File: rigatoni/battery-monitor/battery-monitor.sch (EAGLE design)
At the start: 35 parts, among them J1 S2B-XH-A_(LF)(SN), J2 XF2C-2555-41A, J4 S4B-XH-A(LF)(SN), U1 LT1930ES5TRMPBF_BOOST_CONV, U2 ETH-POE, U3 STM32H743ZIT6

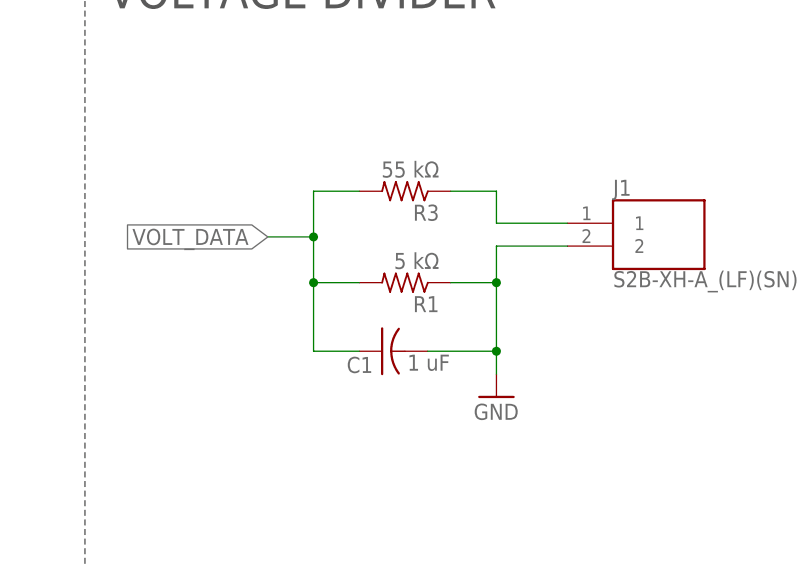
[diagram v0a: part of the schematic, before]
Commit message: Fix R1 value
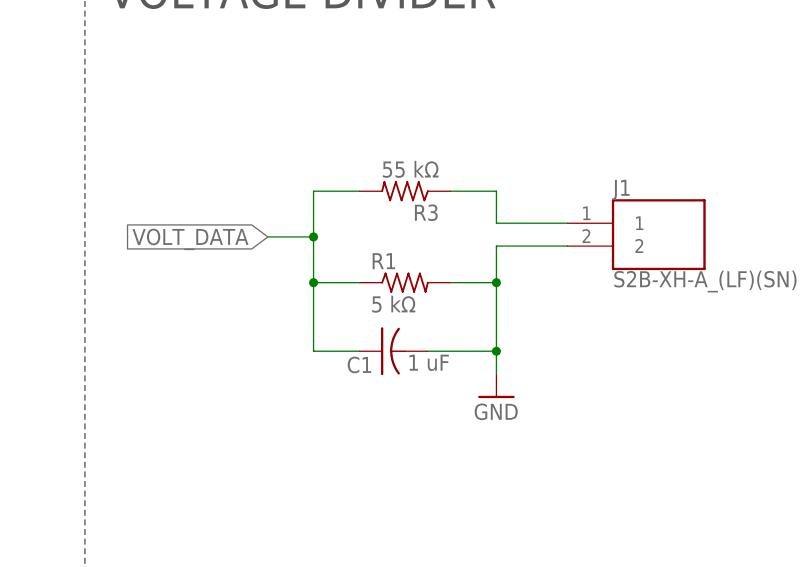
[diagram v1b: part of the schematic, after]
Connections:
- net GND: now also R1.2; no longer R1.1
- net VOLT_DATA: now also R1.1; no longer R1.2
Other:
- moved on the sheet: R1
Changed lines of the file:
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@@
 <setting verticaltext="up"/>
 </settings>
-<grid distance="0.1" unitdist="inch" unit="inch" style="lines" multiple="1" display="yes" altdistance="0.01" altunitdist="inch" altunit="inch"/>
+<grid distance="0.1" unitdist="inch" unit="inch" style="lines" multiple="1" display="no" altdistance="0.01" altunitdist="inch" altunit="inch"/>
 <layers>
 <layer number="1" name="Top" color="4" fill="1" visible="no" active="no"/>
@@
 </part>
 <part name="U3" library="RoboRacing_STM" deviceset="STM32H743ZIT6" device=""/>
-<part name="R1" library="rcl" library_urn="urn:adsk.eagle:library:334" deviceset="R-US_" device="R0603" package3d_urn="urn:adsk.eagle:package:23555/3" value="5 kΩ"/>
 <part name="R3" library="rcl" library_urn="urn:adsk.eagle:library:334" deviceset="R-US_" device="R0603" package3d_urn="urn:adsk.eagle:package:23555/3" value="55 kΩ"/>
 <part name="J1" library="drive_brake" deviceset="S2B-XH-A_(LF)(SN)" device=""/>
@@
 <part name="C1" library="rcl" library_urn="urn:adsk.eagle:library:334" deviceset="C-US" device="C0603" package3d_urn="urn:adsk.eagle:package:23616/2" value="1 uF"/>
 <part name="J2" library="con-omron" library_urn="urn:adsk.eagle:library:167" deviceset="XF2*-25?" device="55-41A" package3d_urn="urn:adsk.eagle:package:9078/1" technology="C"/>
+<part name="R1" library="rcl" library_urn="urn:adsk.eagle:library:334" deviceset="R-US_" device="R0603" package3d_urn="urn:adsk.eagle:package:23555/3" value="5 kΩ"/>
 </parts>
 <sheets>
@@
 <attribute name="VALUE" x="385.8006" y="113.2586" size="2.0828" layer="96" ratio="6" rot="SR0"/>
 </instance>
-<instance part="R1" gate="G$1" x="264.16" y="25.4" smashed="yes" rot="R180">
-<attribute name="NAME" x="267.97" y="23.9014" size="1.778" layer="95" rot="R180"/>
-<attribute name="VALUE" x="267.97" y="28.702" size="1.778" layer="96" rot="R180"/>
-</instance>
 <instance part="R3" gate="G$1" x="264.16" y="35.56" smashed="yes" rot="R180">
 <attribute name="NAME" x="267.97" y="34.0614" size="1.778" layer="95" rot="R180"/>
@@
 <instance part="J2" gate="-25" x="342.9" y="-2.54" smashed="yes">
 <attribute name="NAME" x="345.44" y="-3.302" size="1.524" layer="95"/>
+</instance>
+<instance part="R1" gate="G$1" x="264.16" y="25.4" smashed="yes">
+<attribute name="NAME" x="260.35" y="26.8986" size="1.778" layer="95"/>
+<attribute name="VALUE" x="260.35" y="22.098" size="1.778" layer="96"/>
 </instance>
 </instances>
@@
 </segment>
 <segment>
-<pinref part="R1" gate="G$1" pin="1"/>
 <wire x1="269.24" y1="25.4" x2="274.32" y2="25.4" width="0.1524" layer="91"/>
 <pinref part="J1" gate="G$1" pin="2"/>
@@
 <wire x1="266.7" y1="17.78" x2="274.32" y2="17.78" width="0.1524" layer="91"/>
 <junction x="274.32" y="17.78"/>
+<pinref part="R1" gate="G$1" pin="2"/>
 </segment>
 </net>
@@
 <pinref part="R3" gate="G$1" pin="2"/>
 <wire x1="259.08" y1="35.56" x2="254" y2="35.56" width="0.1524" layer="91"/>
-<pinref part="R1" gate="G$1" pin="2"/>
 <wire x1="254" y1="35.56" x2="254" y2="30.48" width="0.1524" layer="91"/>
 <wire x1="254" y1="30.48" x2="254" y2="25.4" width="0.1524" layer="91"/>
@@
 <wire x1="254" y1="17.78" x2="259.08" y2="17.78" width="0.1524" layer="91"/>
 <pinref part="C1" gate="G$1" pin="1"/>
-</segment>
-<segment>
+<pinref part="R1" gate="G$1" pin="1"/>
+</segment>
+<segment>

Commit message: Removed Ethernet Header and MCU from schematic
Also updated RoboRacing_STM library
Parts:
- removed C14: 1uF, rcl:C-USC0603
- removed C15: 0.1uF, rcl:C-USC0603
- removed D6: 5.1V, SparkFun-DiscreteSemi:DIODE-ZENER-MM3Z3V3T1G
- removed D7: (no value), RoboJackets-Diodes:SCHOTTKYSOD-323
- removed F1: 0.3A, RoboJackets-Passive:FUSE1206
- removed J2: XF2C-2555-41A, con-omron:XF2C-2555-41A
- removed LD2: GREEN, SparkFun:LED0603
- removed R10: 10kΩ, rcl:R-US_R0603
- removed U2: ETH-POE, ethernet_poe:ETH-POE
- removed U3: STM32H743ZIT6, RoboRacing_STM:STM32H743ZIT6
- added J3: STM32H743ZIT6_HEADER, RoboRacing_STM:STM32H743ZIT6_HEADER
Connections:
- removed net ETH_RST: U2.RSTN
- removed net INT_ETH: U2.INTN
- removed net MISO: U2.MISO
- removed net MOSI: U2.MOSI
- removed net N$10: D7.A, F1.1
- removed net N$4: F1.2, U2.+5V
- removed net SCLK: U2.SCLK
- removed net SCNN: R10.1, U2.SCSN
- net +5V: no longer C14.1, C15.1, D6.C, D7.C, LD2.A, R10.2
- net CURR_DATA: now also J3.17; no longer U3A.PA2
- net GND: no longer C14.2, C15.2, D6.A, LD2.C, U2.GND
- net VOLT_DATA: now also J3.19; no longer U3A.PA1
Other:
- note removed: "ETHERNET HEADER"
- note removed: "ETHERNET LED"

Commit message: Updated Schematic with new Nucleo Header
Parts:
- removed J3: STM32H743ZIT6_HEADER, RoboRacing_STM:STM32H743ZIT6_HEADER
- added U2: NUCLEO-H743ZI-HEADER, RoboRacing_STM:NUCLEO-H743ZI-HEADER
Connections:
- net CURR_DATA: now also U2G$4.A0/ADC123_IN3; no longer J3.17
- net VOLT_DATA: now also U2G$4.A1/ADC123_IN10; no longer J3.19
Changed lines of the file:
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@@
 <part name="C1" library="rcl" library_urn="urn:adsk.eagle:library:334" deviceset="C-US" device="C0603" package3d_urn="urn:adsk.eagle:package:23616/2" value="1 uF"/>
 <part name="R1" library="rcl" library_urn="urn:adsk.eagle:library:334" deviceset="R-US_" device="R0603" package3d_urn="urn:adsk.eagle:package:23555/3" value="5 kΩ"/>
-<part name="J3" library="RoboRacing_STM" deviceset="STM32H743ZIT6_HEADER" device=""/>
+<part name="U2" library="RoboRacing_STM" deviceset="NUCLEO-H743ZI-HEADER" device=""/>
 </parts>
 <sheets>
@@
 <attribute name="VALUE" x="260.35" y="22.098" size="1.778" layer="96"/>
 </instance>
-<instance part="J3" gate="A" x="419.1" y="43.18" smashed="yes">
-<attribute name="NAME" x="387.35" y="69.215" size="1.778" layer="95"/>
-<attribute name="VALUE" x="387.35" y="-0.508" size="1.778" layer="96" align="top-left"/>
+<instance part="U2" gate="G$1" x="30.48" y="226.06" smashed="yes">
+<attribute name="NAME" x="17.78" y="283.21" size="1.778" layer="95"/>
+<attribute name="VALUE" x="17.78" y="168.91" size="1.778" layer="96" rot="MR180"/>
+</instance>
+<instance part="U2" gate="G$2" x="96.52" y="223.52" smashed="yes">
+<attribute name="NAME" x="83.82" y="280.67" size="1.778" layer="95"/>
+<attribute name="VALUE" x="83.82" y="168.91" size="1.778" layer="96" rot="MR180"/>
+</instance>
+<instance part="U2" gate="G$3" x="200.66" y="256.54" smashed="yes">
+<attribute name="NAME" x="172.72" y="278.13" size="1.778" layer="95"/>
+<attribute name="VALUE" x="172.72" y="237.49" size="1.778" layer="96" rot="MR180"/>
+</instance>
+<instance part="U2" gate="G$4" x="203.2" y="193.04" smashed="yes">
+<attribute name="NAME" x="175.26" y="222.25" size="1.778" layer="95"/>
+<attribute name="VALUE" x="175.26" y="166.37" size="1.778" layer="96" rot="MR180"/>
+</instance>
+<instance part="U2" gate="G$5" x="317.5" y="256.54" smashed="yes">
+<attribute name="NAME" x="284.48" y="280.67" size="1.778" layer="95"/>
+<attribute name="VALUE" x="284.48" y="234.95" size="1.778" layer="96" rot="MR180"/>
+</instance>
+<instance part="U2" gate="G$6" x="312.42" y="190.5" smashed="yes">
+<attribute name="NAME" x="284.48" y="224.79" size="1.778" layer="95"/>
+<attribute name="VALUE" x="284.48" y="158.75" size="1.778" layer="96" rot="MR180"/>
 </instance>
 </instances>
@@
 </segment>
 <segment>
-<pinref part="J3" gate="A" pin="17"/>
-<wire x1="391.16" y1="38.1" x2="381" y2="38.1" width="0.1524" layer="91"/>
-<label x="381" y="38.1" size="1.778" layer="95" rot="R180" xref="yes"/>
+<pinref part="U2" gate="G$4" pin="A0/ADC123_IN3"/>
+<wire x1="170.18" y1="215.9" x2="165.1" y2="215.9" width="0.1524" layer="91"/>
+<label x="165.1" y="215.9" size="1.778" layer="95" rot="R180" xref="yes"/>
 </segment>
 </net>
@@
 </segment>
 <segment>
-<pinref part="J3" gate="A" pin="19"/>
-<wire x1="391.16" y1="35.56" x2="373.38" y2="35.56" width="0.1524" layer="91"/>
-<label x="381" y="25.4" size="1.778" layer="95" rot="R180" xref="yes"/>
-</segment>
-</net>
+<pinref part="U2" gate="G$4" pin="A1/ADC123_IN10"/>
+<wire x1="170.18" y1="213.36" x2="147.32" y2="213.36" width="0.1524" layer="91"/>
+<label x="147.32" y="213.36" size="1.778" layer="95" rot="R180" xref="yes"/>
+</segment>
+</net>

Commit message: Added 12V to 5V power circuit and LCD connector to schematic
Started to assign pins between the LCD connector and the nucleo header pins
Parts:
- added C2: 10uF, rcl:C-US025-024X044
- added C3: 0.1uF, rcl:C-US025-024X044
- added C4: 100uF, rcl:C-US025-024X044
- added D5: Yellow, RoboJackets-LEDs:LED-YELLOW0603
- added D6: GREEN, RoboJackets-LEDs:LED-GREEN1206
- added F1: 630mA, RoboJackets-Fuses:SMD_FUSE0603
- added F2: 1.875A, RoboJackets-Fuses:SMD_FUSE0603
- added J2: QSH-030-01-X-D-A-XX, QSH-030-01-X-D-A-XX:QSH-030-01-X-D-A-XX
- added J3: (no value), RoboJackets-Connectors:PJ-037A
- added Q1: STT4P3LLH6, RoboJackets-Discrete:STT4P3LLH6
- added R5: 1k, rcl:R-US_R0603
- added TVS_1: D5V0L1B2WS-7, RoboJackets-Diodes:D5V0L1B2WS-7
- added U3: TPSM84205EAB, RoboRacing_STM:TPSM84205EAB
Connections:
- new net 5V_MAIN: C4.1, F2.1, U3.VOUT
- new net BLGND: J2.27
- new net BLGND_2: J2.29
- new net BLVDD(+5V): J2.21
- new net BLVDD_2(+5V): J2.23
- new net BL_CTRL: J2.53
- new net DSI_CK_N: J2.05, U2G$6.D5/TIMER_A_PWM2
- new net DSI_CK_P: J2.03, U2G$6.D6/TIMER_A_PWM1
- new net DSI_D0_N: J2.11, U2G$6.D2/IO
- new net DSI_D0_P: J2.09, U2G$5.D8/IO
- new net DSI_D1_N: J2.17, U2G$6.D7/IO
- new net DSI_D1_P: J2.15, U2G$6.D4/IO
- new net DSI_TE: J2.49
- new net I2C_SCL: J2.44
- new net I2C_SDA: J2.40
- new net N$10: D5.C, Q1.D
- new net N$11: D6.A, F2.2
- new net N$2: D5.A, F1.2
- new net N$3: Q1.G, R5.2
- new net N$4: C2.1, Q1.S, TVS_1.C, U3.VIN
- new net N$7: F1.1, J3.1
- new net RESET: J2.57
- new net TOUCH_INT: J2.04
- new net VDD(2.8V-3.3V): J2.36
- net +5V: now also C3.1, D6.C, U2G$1.E5V
- net GND: now also C2.2, C3.2, C4.2, J2.01, J2.07, J2.13, J2.19, J3.2, R5.1, TVS_1.A, U2G$1.GND_CN11, U3.GND
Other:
- note added: "*Note: C2 should be rated @ 25V"
- note added: "MCU HEADER"
- note added: "POWER 12V to 5V"
- note added: "· TPSM84205EAB DC/DC Converter"
- moved on the sheet: C1, C10, C11, C18, C7, C8, C9, D1, D2, D3, D4, J1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
